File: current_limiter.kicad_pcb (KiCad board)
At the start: 2 copper layers, 56.9 x 25.9 mm, 31 parts, among them J1 VIN, J2 VOUT, Q1 BSC040N10NS5, Q2 BC849, Q3 BC858, U1 TLV1805QDBVRQ1, U2 INA181A2IDBVR, U3 LM8261

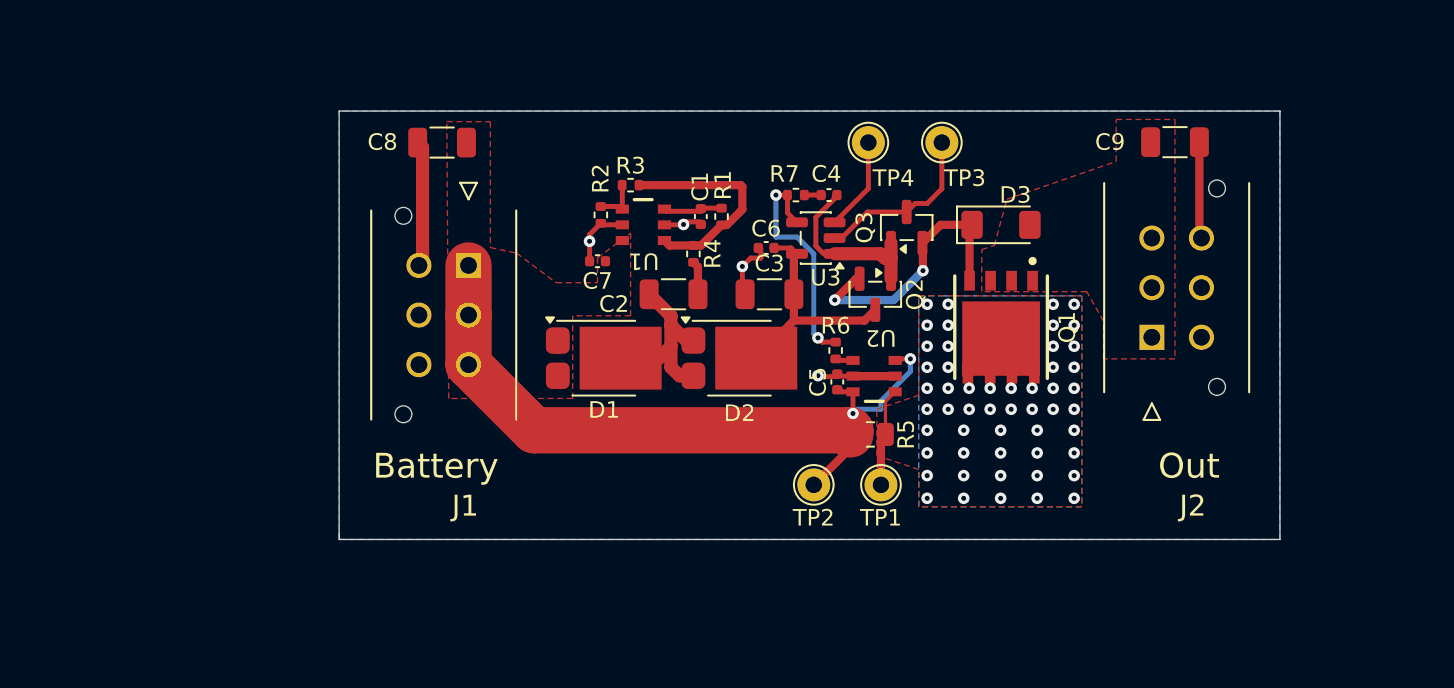
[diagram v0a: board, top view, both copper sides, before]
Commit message: version 2: changed opamp & diodes to more responsible components, changed reference voltage
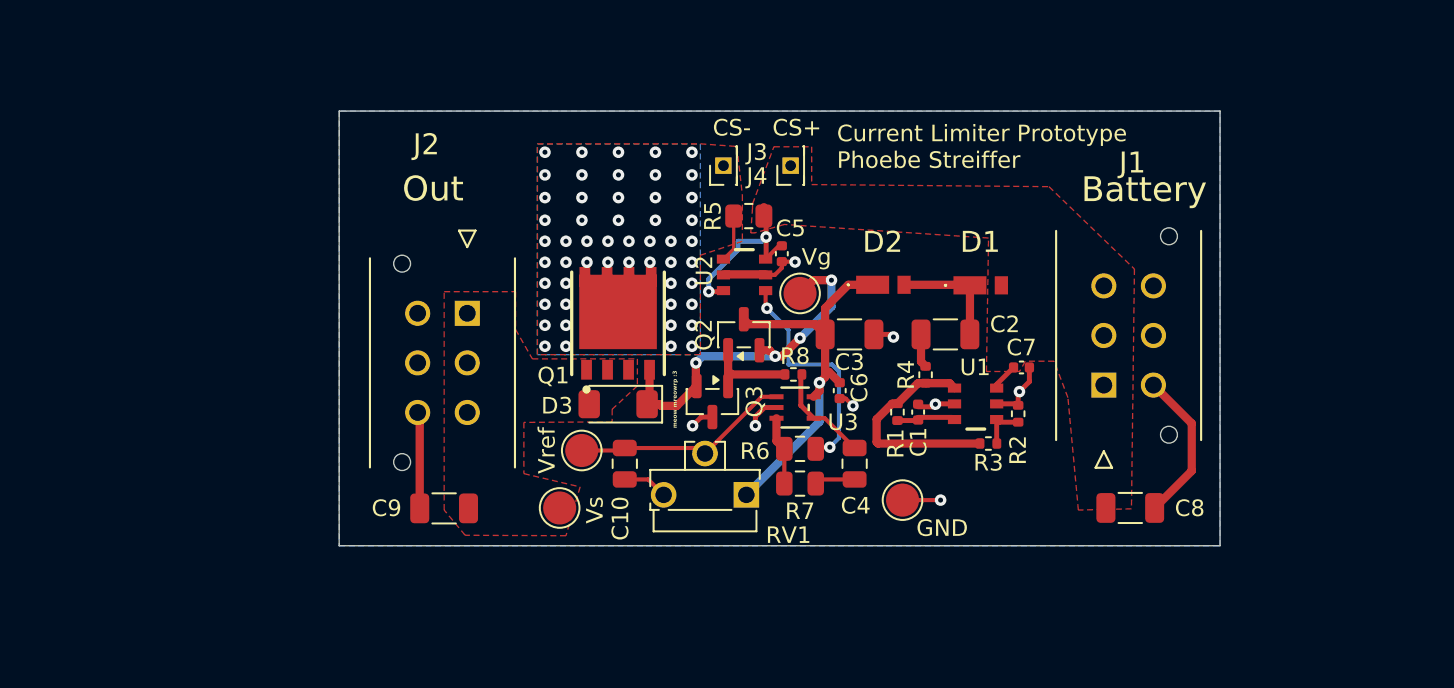
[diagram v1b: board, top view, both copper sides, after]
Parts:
- removed TP1: CurrentSense-, TestPoint:TestPoint_THTPad_D2.0mm_Drill1.0mm
- removed TP2: CurrentSense+, TestPoint:TestPoint_THTPad_D2.0mm_Drill1.0mm
- added C10: 100n, Capacitor_SMD:C_0805_2012Metric, F.Cu at (127.0, 51.3)
- added J3: CS-, Connector_PinHeader_1.27mm:PinHeader_1x01_P1.27mm_Vertical, F.Cu at (133.0, 33.3)
- added J4: CS+, Connector_PinHeader_1.27mm:PinHeader_1x01_P1.27mm_Vertical, F.Cu at (137.0, 33.3)
- added R8: 10, Resistor_SMD:R_0402_1005Metric, F.Cu at (137.2, 45.9)
- added RV1: R_Potentiometer_Trim_US, Potentiometer_THT:Potentiometer_Runtron_RM-063_Horizontal, F.Cu at (134.4, 53.2)
- added TP5: Vg, TestPoint:TestPoint_Pad_D2.0mm, F.Cu at (137.6, 41.0)
- added TP6: Vs, TestPoint:TestPoint_Pad_D2.0mm, F.Cu at (123.1, 54.0)
- C4: footprint Capacitor_SMD:C_0402_1005Metric -> Capacitor_SMD:C_0805_2012Metric
- D1, D2: value PMEG050V030EPD -> CUHS20S40; footprint Package_TO_SOT_SMD:Nexperia_CFP15_SOT-1289 -> Current_Limiter_Stuff:CUHS20S40
- R6, R7: footprint Resistor_SMD:R_0402_1005Metric -> Capacitor_SMD:C_0805_2012Metric
- TP3: value GND -> Vref; footprint TestPoint:TestPoint_THTPad_D2.0mm_Drill1.0mm -> TestPoint:TestPoint_Pad_D2.0mm
- TP4: value Vref -> GND; footprint TestPoint:TestPoint_THTPad_D2.0mm_Drill1.0mm -> TestPoint:TestPoint_Pad_D2.0mm
- U3: value LM8261 -> OPA991IDCKR; footprint Package_TO_SOT_SMD:SOT-23-5 -> Current_Limiter_Stuff:SC_91IDCKR_TEX
- moved C9 49.4 mm to (116.1, 54.0), turned to 180 degrees
- moved C8 47.1 mm to (157.6, 54.0), turned to 0 degrees
- moved J2 41.4 mm to (117.5, 42.2), turned to 90 degrees
- moved J1 39.1 mm to (156.0, 46.5), turned to -90 degrees
- moved TP3 28.7 mm to (124.4, 50.5), turned to 0 degrees
- moved R2 28.0 mm to (150.8, 48.3), turned to -90 degrees
- moved R3 26.7 mm to (149.0, 50.1), turned to 180 degrees
- moved C7 26.4 mm to (151.0, 45.5), turned to 0 degrees
- moved D3 25.6 mm to (126.6, 47.7), turned to 180 degrees
- moved D1 23.2 mm to (148.5, 40.5)
- moved Q1 23.2 mm to (126.6, 42.8), turned to 90 degrees
- moved U1 22.8 mm to (148.2, 47.7), turned to 0 degrees
- moved TP4 21.7 mm to (143.8, 53.5), turned to 0 degrees
- moved C1 17.7 mm to (144.7, 48.2), turned to -90 degrees
- moved R7 17.4 mm to (137.6, 52.5)
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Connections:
- D1 pad 1: +15V -> /pump flying
- D2 pad 1: /pump flying -> VCC
- Q2 pad 1: /PI_OUT -> /BASE
- Q3 pad 1: /PI_OUT -> /BASE
- TP3 pad 1: GND -> /REF_SET
- TP4 pad 1: /REF_SET -> GND
- U3 pad 1: /PI_OUT -> /REF_SET
- U3 pad 3: /REF_SET -> /PI_IN-
- U3 pad 4: /PI_IN- -> /PI_OUT
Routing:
- net +15V: track 46.1 -> 13.0 mm
- net /CS_OUT: track 1.09 -> 14.0 mm, vias 0 -> 2
- net /PI_IN-: track 14.2 -> 4.15 mm, vias 2 -> 0
- net VCC: track 14.7 -> 24.2 mm, vias 0 -> 1
- net /REF_SET: track 5.67 -> 13.4 mm
- net /BASE: track 0.00 -> 5.69 mm
- net /FET_EN: track 17.0 -> 21.9 mm, vias 2 -> 4
- net /pump flying: track 11.6 -> 6.97 mm
- net /PI_OUT: track 10.6 -> 6.22 mm
- net /CSA_IN-: track 6.30 -> 3.53 mm
- net GND: track 38.6 -> 37.2 mm, vias 4 -> 8
- net Net-(C4-Pad2): track 1.17 -> 2.45 mm
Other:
- board size 56.9 x 25.9 mm -> 53.3 x 26.3 mm
- board text added: "Current Limiter Prototype Phoebe Streiffer"
- board text added: "meow mreowrp :3"

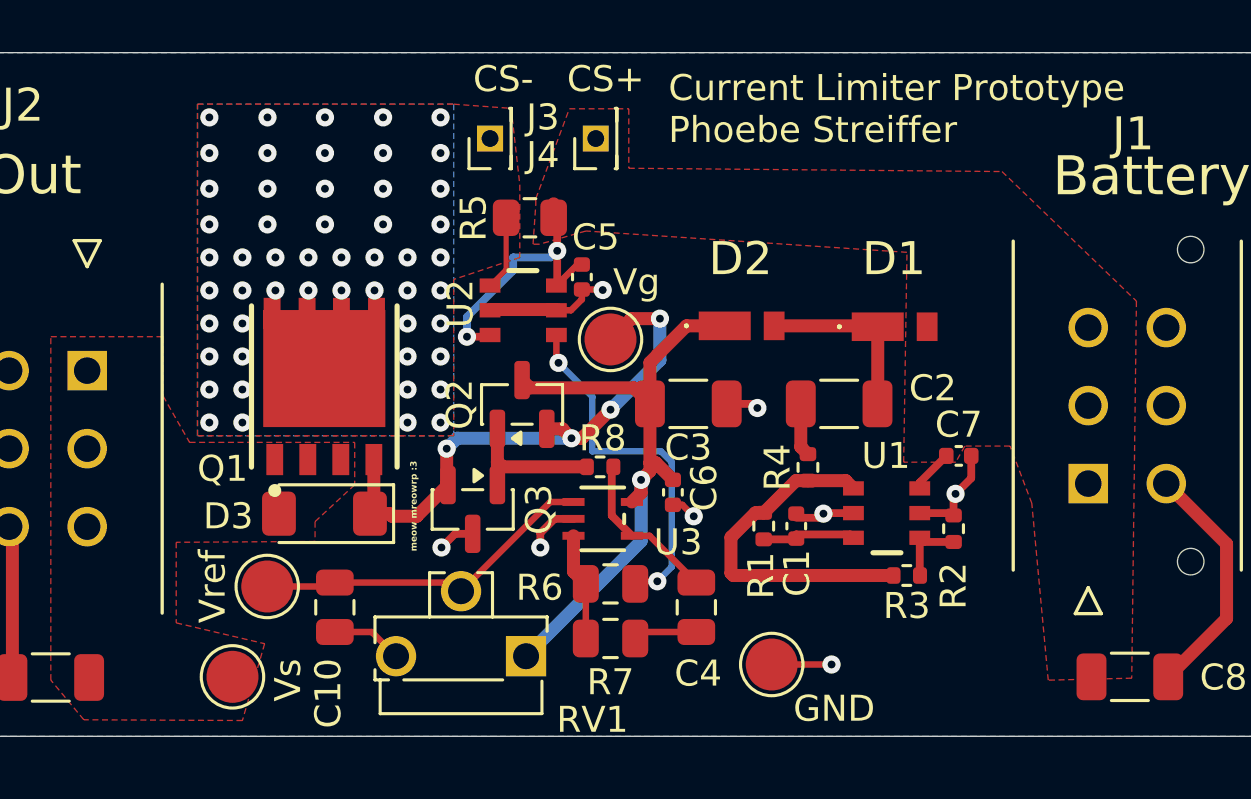
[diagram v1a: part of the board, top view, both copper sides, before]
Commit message: minor updates, moved caps around + added resistor for current limiting
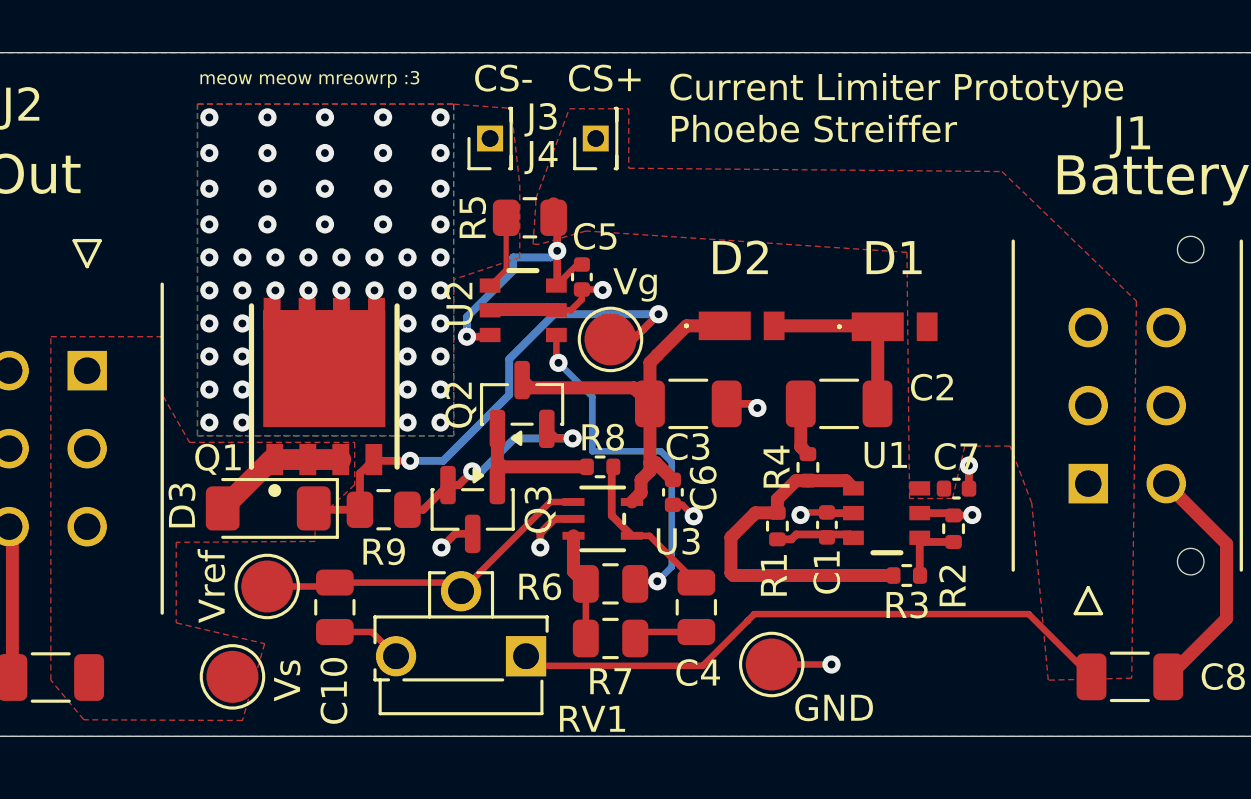
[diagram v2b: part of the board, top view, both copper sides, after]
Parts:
- added R9: 0, Resistor_SMD:R_0805_2012Metric, F.Cu at (128.9, 47.5)
- moved D3 2.17 mm to (124.4, 47.5)
- moved C7 1.26 mm to (150.9, 46.7)
- moved C1 1.18 mm to (145.9, 48.1)
- moved R1 0.53 mm to (144.0, 48.2)
- turned C10 to 90 degrees
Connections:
- net /Vout renamed /VBATT
- C10 pad 1: /REF_SET -> GND
- C10 pad 2: GND -> /REF_SET
- D3 pad 1: /FET_EN -> /fet_gate
- Q1 pad 4: /FET_EN -> /fet_gate
- Q2 pad 2: /FET_EN -> Net-(Q2-E)
- Q3 pad 2: /FET_EN -> Net-(Q2-E)
- RV1 pad 1: VCC -> +15V
- TP5 pad 1: /FET_EN -> /fet_gate
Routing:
- net +15V: track 13.0 -> 35.1 mm
- net /FET_EN: track 21.9 -> 0.00 mm, vias 4 -> 0
- net /fet_gate: track 0.00 -> 20.3 mm, vias 0 -> 2
- net Net-(Q2-E): track 0.00 -> 8.79 mm, vias 0 -> 2
- net VCC: track 24.2 -> 15.6 mm, vias 1 -> 0
- net /VBATT: track 0.00 -> 5.32 mm
- net GND: track 37.2 -> 36.2 mm, vias 8 -> 9
- net /OSC_IN+: track 3.58 -> 3.06 mm
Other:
- board text added: "meow meow mreowrp :3"
- board text removed: "meow mreowrp :3"

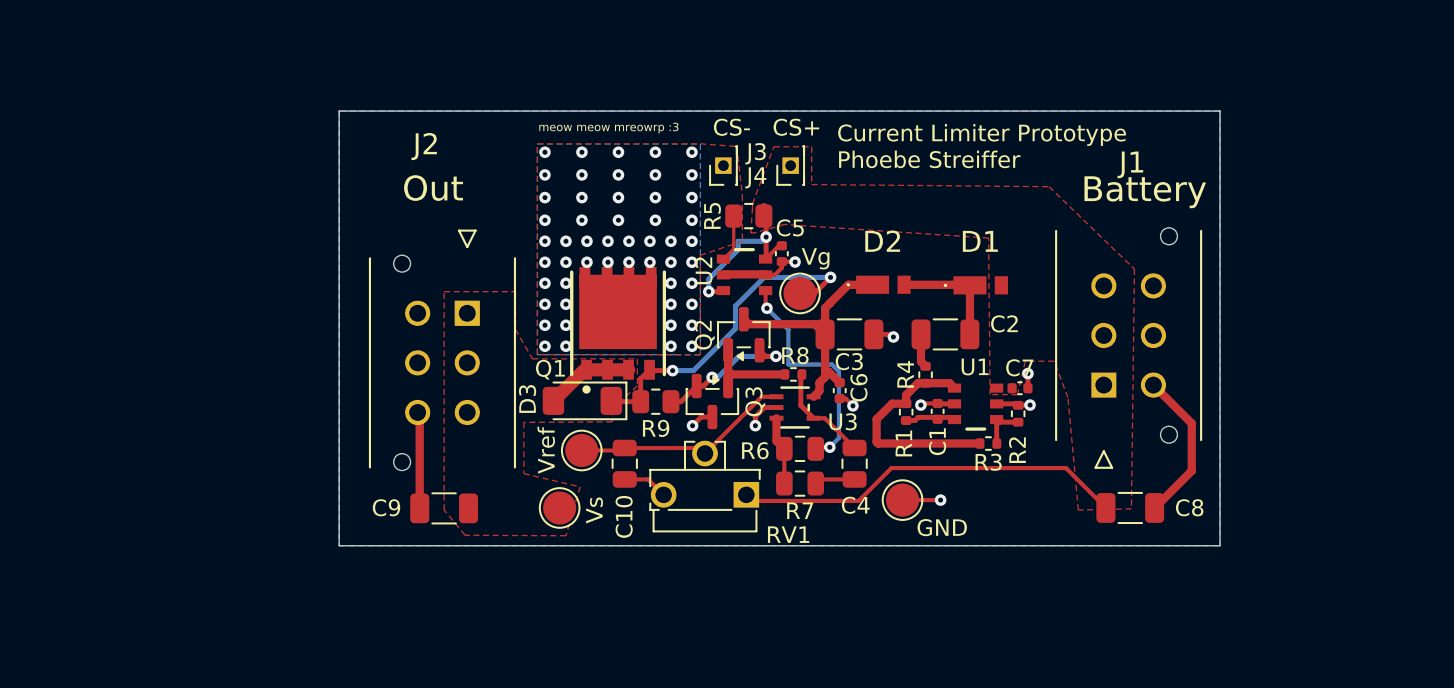
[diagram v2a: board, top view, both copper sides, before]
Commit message: minor updates, added second zener to cap negative Vgs and DNP diode for potential minimum opamp output
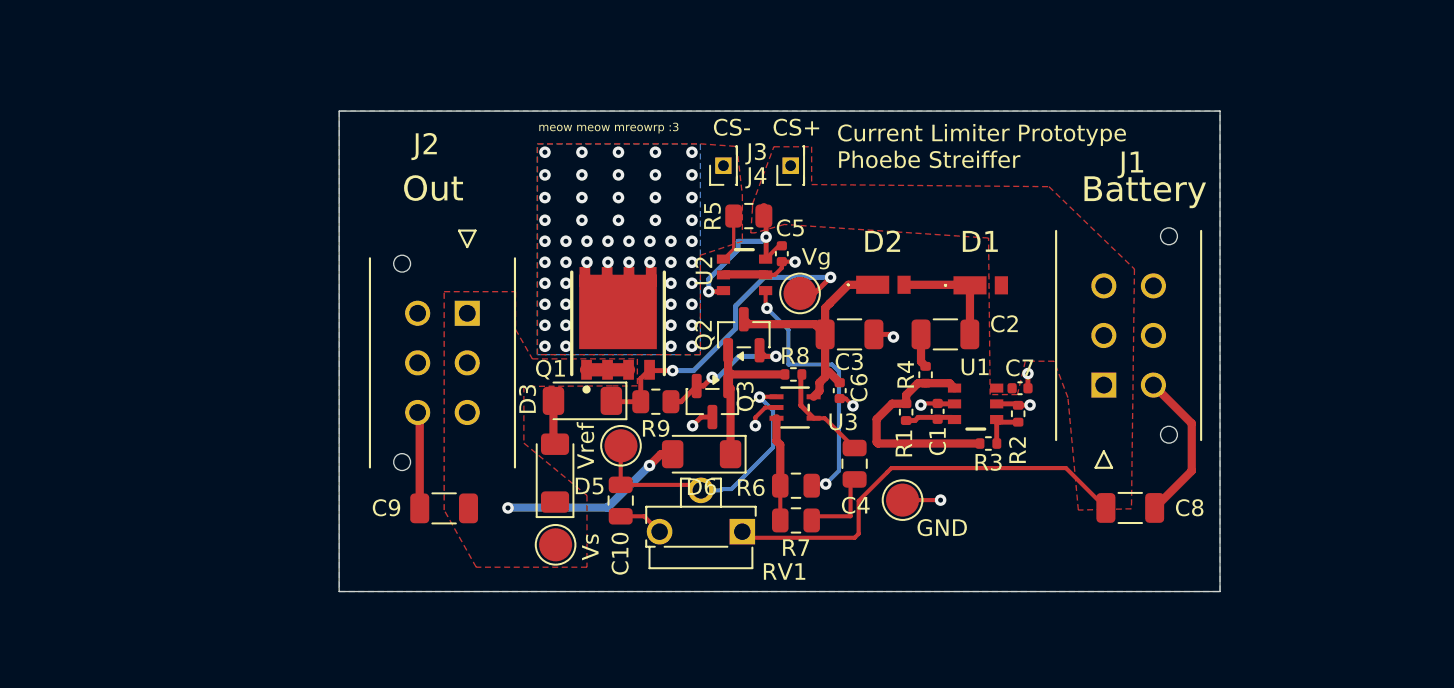
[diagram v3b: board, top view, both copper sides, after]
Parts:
- added D5: BZV55B20, Diode_SMD:D_MiniMELF, F.Cu at (122.8, 51.9)
- added D6: BZV55B20, Diode_SMD:D_MiniMELF, F.Cu at (131.6, 50.7)
- moved TP3 2.39 mm to (126.8, 50.2)
- moved R6 2.24 mm to (137.4, 52.6)
- moved R7 2.24 mm to (137.4, 54.7)
- moved TP6 2.24 mm to (122.8, 56.2)
- moved C10 2.24 mm to (126.8, 53.5)
- moved RV1 2.24 mm to (134.1, 55.4)
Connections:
- D3 pad 2: /VBATT -> Net-(D3-A)
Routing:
- net /VBATT: track 5.32 -> 14.0 mm, vias 0 -> 2
- net /BASE: track 5.69 -> 9.87 mm
- net /REF_SET: track 13.4 -> 17.4 mm, vias 0 -> 1
- net Net-(D3-A): track 0.00 -> 2.66 mm
- net Net-(C4-Pad2): track 2.45 -> 4.78 mm
- net /CS_OUT: track 14.0 -> 16.3 mm
- net +15V: track 35.1 -> 37.4 mm
- net /PI_IN-: track 4.15 -> 6.27 mm
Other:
- board size 53.3 x 26.3 mm -> 53.3 x 29.1 mm

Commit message: version 3: updated to 4-layer board, added shunts + various current-limiting resistors, changed reference to have maximum value of 5A
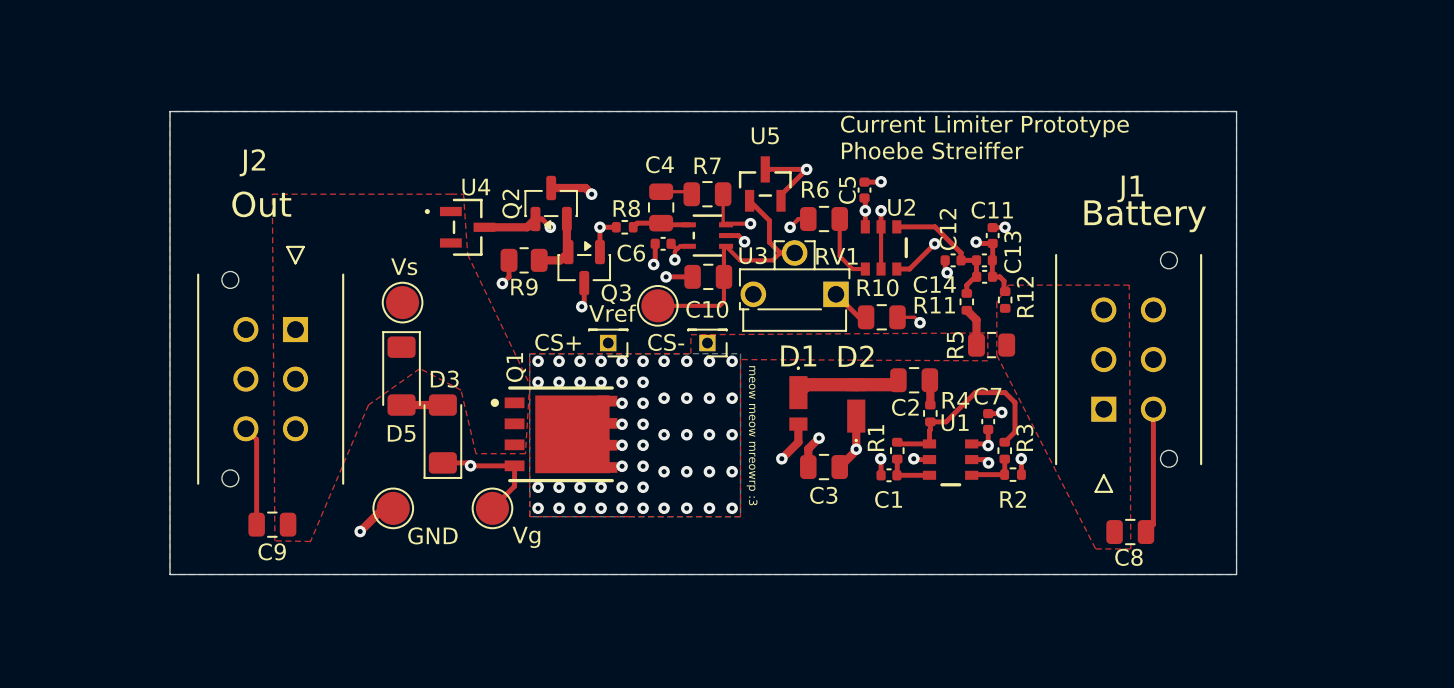
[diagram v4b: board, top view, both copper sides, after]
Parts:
- removed D6: BZV55B20, Diode_SMD:D_MiniMELF
- added C11: 470n, Capacitor_SMD:C_0402_1005Metric, F.Cu at (149.2, 37.5)
- added C12: 470n, Capacitor_SMD:C_0402_1005Metric, F.Cu at (146.9, 39.0)
- added C13: 10u, Capacitor_SMD:C_0402_1005Metric, F.Cu at (148.8, 39.0)
- added C14: 10u, Capacitor_SMD:C_0402_1005Metric, F.Cu at (148.8, 40.0)
- added R10: 50k, Capacitor_SMD:C_0805_2012Metric, F.Cu at (142.5, 42.4)
- added R11: 10, Resistor_SMD:R_0402_1005Metric, F.Cu at (147.7, 41.5)
- added R12: 10, Resistor_SMD:R_0402_1005Metric, F.Cu at (150.0, 41.4)
- added U4: BAT54CLT3G, Current_Limiter_Stuff:SOT-23-3_1P4X3P040_ONS, F.Cu at (117.5, 37.0)
- added U5: LM4040DIM3-2.5/NOPB, Current_Limiter_Stuff:DBZ3, F.Cu at (135.5, 34.4)
- C2, C3, C8, C9: footprint Capacitor_SMD:C_1206_3216Metric -> Capacitor_SMD:C_0805_2012Metric
- moved TP4 30.8 mm to (113.0, 54.0)
- moved TP5 22.7 mm to (119.0, 54.0)
- moved R7 20.4 mm to (132.0, 35.0), turned to 0 degrees
- moved C4 19.4 mm to (129.2, 35.8), turned to 90 degrees
- moved TP6 17.3 mm to (113.6, 41.6), turned to 90 degrees
- moved R5 16.6 mm to (149.2, 44.1)
- moved R6 16.2 mm to (139.1, 36.5)
- moved RV1 15.4 mm to (139.8, 41.1)
- moved J4 15.4 mm to (126.0, 44.0), turned to 180 degrees
- moved C10 14.5 mm to (132.1, 40.0), turned to 0 degrees
- moved Q2 14.1 mm to (122.5, 35.6)
- moved C6 13.9 mm to (129.3, 38.0), turned to 0 degrees
- moved R8 13.5 mm to (127.0, 37.0)
- moved D1 13.1 mm to (137.5, 47.6), turned to -90 degrees
- moved R9 11.7 mm to (120.9, 39.0)
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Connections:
- RV1 pad 1: +15V -> Net-(R10-Pad1)
- U2 pad 3: +15V -> /CS_FILTERED+
- U2 pad 4: /CSA_IN- -> /CS_FILTERED-
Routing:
- net +15V: track 37.4 -> 8.02 mm, vias 2 -> 4
- net VCC: track 15.6 -> 30.8 mm, vias 0 -> 3
- net /VBATT: track 14.0 -> 0.00 mm, vias 2 -> 0
- net /CS_OUT: track 16.3 -> 4.12 mm, vias 2 -> 0
- net /CS_FILTERED+: track 0.00 -> 10.2 mm, vias 0 -> 2
- net /CS_FILTERED-: track 0.00 -> 8.03 mm
- net Net-(Q2-E): track 8.79 -> 4.02 mm, vias 2 -> 0
- net GND: track 36.2 -> 40.2 mm, vias 9 -> 16
- net Net-(C4-Pad2): track 4.78 -> 1.91 mm
- net Net-(R10-Pad1): track 0.00 -> 2.71 mm
- net /PI_OUT: track 6.22 -> 3.51 mm
- net /OSC_OUT: track 13.7 -> 12.1 mm
- net /PI_IN-: track 6.27 -> 7.72 mm, vias 0 -> 2
- net /REF_SET: track 17.4 -> 16.1 mm, vias 1 -> 0
- net /CSA_IN-: track 3.53 -> 2.35 mm
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- added copper zone on In1.Cu, net +15V
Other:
- board size 53.3 x 29.1 mm -> 64.5 x 28 mm
- copper layers 2 -> 4
